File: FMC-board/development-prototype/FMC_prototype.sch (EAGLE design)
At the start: 68 parts, among them J1 DC_POWER_JACK-PJ-102AH, J2 DC_POWER_JACK-PJ-102AH

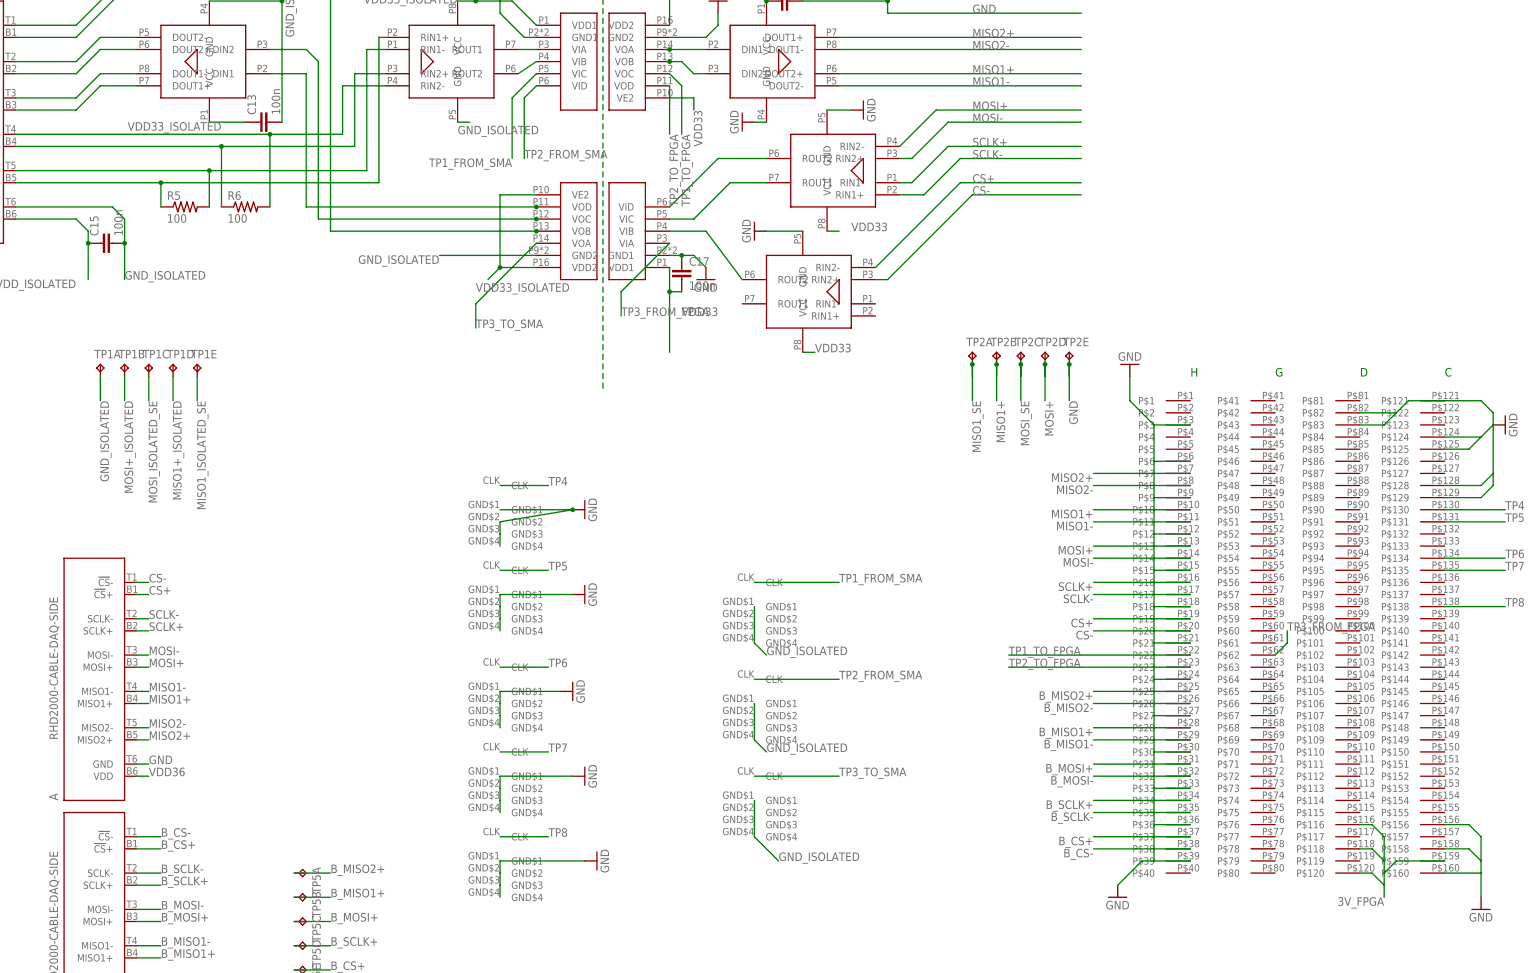
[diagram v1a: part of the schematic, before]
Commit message: clearing all but layer setup and silkscreen overlap warnings
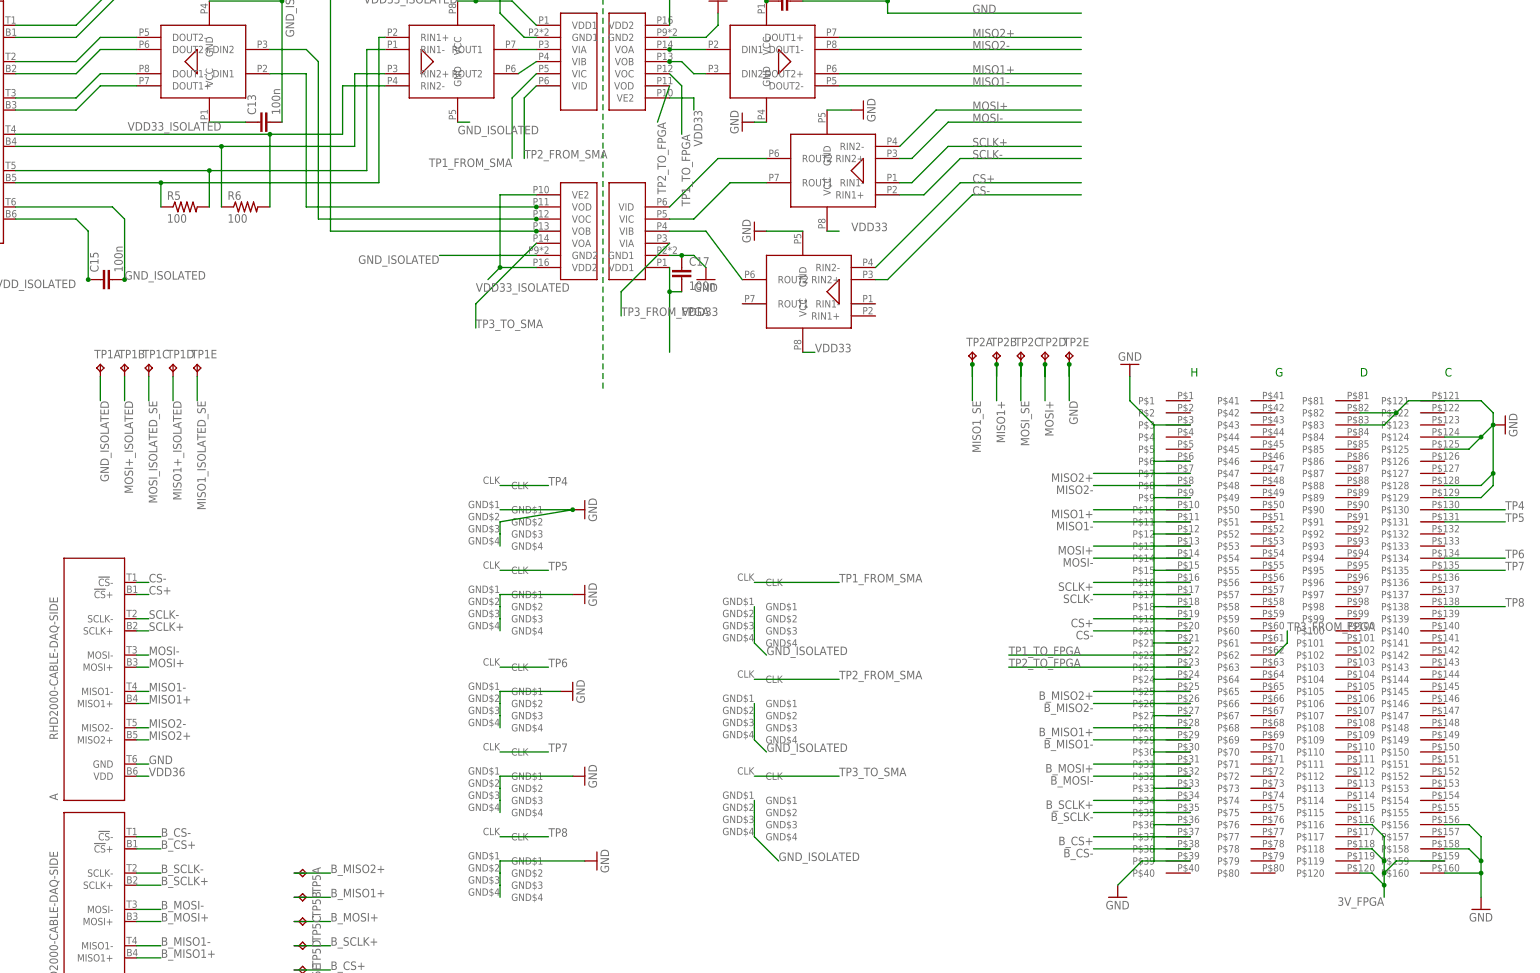
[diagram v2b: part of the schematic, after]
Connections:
- removed net GND4: C15.2
- net GND_ISOLATED: now also C15.2
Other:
- moved on the sheet: C15
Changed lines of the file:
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@@
 <instance part="C13" gate="C" x="91.44" y="203.2" rot="R90"/>
 <instance part="C14" gate="C" x="91.44" y="233.68" rot="R90"/>
-<instance part="C15" gate="C" x="58.42" y="177.8" rot="R90"/>
+<instance part="C15" gate="C" x="58.42" y="170.18" rot="R90"/>
 <instance part="C16" gate="C" x="137.16" y="233.68" rot="R180"/>
 <instance part="C17" gate="C" x="180.34" y="172.72"/>
@@
 <wire x1="63.5" y1="182.88" x2="60.96" y2="185.42" width="0.1524" layer="91"/>
 <label x="63.5" y="170.18" size="1.778" layer="95"/>
-<wire x1="63.5" y1="182.88" x2="63.5" y2="170.18" width="0.1524" layer="91"/>
+<wire x1="63.5" y1="182.88" x2="63.5" y2="172.72" width="0.1524" layer="91"/>
 <pinref part="A_ISOLATED" gate="A" pin="GND"/>
 <wire x1="60.96" y1="185.42" x2="40.64" y2="185.42" width="0.1524" layer="91"/>
+<pinref part="C15" gate="C" pin="2"/>
+<junction x="63.5" y="170.18"/>
+<wire x1="63.5" y1="172.72" x2="63.5" y2="170.18" width="0.1524" layer="91"/>
 </segment>
 <segment>
@@
 <net name="VDD_ISOLATED" class="0">
 <segment>
-<wire x1="55.88" y1="180.34" x2="55.88" y2="177.8" width="0.1524" layer="91"/>
-<wire x1="55.88" y1="177.8" x2="55.88" y2="170.18" width="0.1524" layer="91"/>
+<wire x1="55.88" y1="180.34" x2="55.88" y2="170.18" width="0.1524" layer="91"/>
 <wire x1="55.88" y1="180.34" x2="53.34" y2="182.88" width="0.1524" layer="91"/>
 <label x="53.34" y="170.18" size="1.778" layer="95" rot="R180"/>
 <pinref part="C15" gate="C" pin="1"/>
-<junction x="55.88" y="177.8"/>
+<junction x="55.88" y="170.18"/>
 <pinref part="A_ISOLATED" gate="A" pin="VDD"/>
 <wire x1="53.34" y1="182.88" x2="40.64" y2="182.88" width="0.1524" layer="91"/>
@@
 <wire x1="347.98" y1="45.72" x2="347.98" y2="40.64" width="0.1524" layer="91"/>
 <pinref part="GND15" gate="1" pin="GND"/>
+<junction x="347.98" y="48.26"/>
+<junction x="347.98" y="45.72"/>
 </segment>
 <segment>
@@
 <wire x1="322.58" y1="139.7" x2="327.66" y2="139.7" width="0.1524" layer="91"/>
 <wire x1="327.66" y1="139.7" x2="330.2" y2="142.24" width="0.1524" layer="91"/>
+<junction x="347.98" y="137.16"/>
+<junction x="350.52" y="129.54"/>
+<junction x="350.52" y="139.7"/>
+<junction x="330.2" y="142.24"/>
 </segment>
 <segment>
@@
 </segment>
 </net>
-<net name="GND4" class="0">
-<segment>
-<pinref part="C15" gate="C" pin="2"/>
-<junction x="63.5" y="177.8"/>
-</segment>
-</net>
 <net name="CS+_ISOLATED" class="0">
 <segment>
@@
 <wire x1="327.66" y1="43.18" x2="327.66" y2="40.64" width="0.1524" layer="91"/>
 <label x="327.66" y="40.64" size="1.778" layer="95" rot="R180"/>
+<junction x="327.66" y="48.26"/>
+<junction x="327.66" y="45.72"/>
+<junction x="327.66" y="43.18"/>
 </segment>
 <segment>
@@
 <segment>
 <pinref part="U$11" gate="G$1" pin="VOD"/>
-<wire x1="177.8" y1="210.82" x2="177.8" y2="200.66" width="0.1524" layer="91"/>
-<label x="177.8" y="200.66" size="1.778" layer="95" rot="R270"/>
-</segment>
-<segment>
+<wire x1="177.8" y1="210.82" x2="175.26" y2="203.2" width="0.1524" layer="91"/>
+<label x="175.26" y="203.2" size="1.778" layer="95" rot="R270"/>
+</segment>
+<segment>

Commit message: added optional DC DC converter
12V > 5V DC DC for powering headstage etc. can still be bypassed with jumper
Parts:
- added C1: 4.7uF, RHD2000_eval_board:C_0603
- added L1: 6.8uH, inductor-neosid:MS42
- added U$20: PDS1, open-ephys:PDS1
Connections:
- new net 12V_FPGA: C1.1, L1.1, U$4G$1.P$155, U$4G$1.P$157
- new net N$1: LINK-5V.3, U$20.+VO
- new net N$2: L1.2, U$20.VIN
- net GND: now also C1.2, U$20.GND
- net GND_ISOLATED: now also U$20.0V
- net VDD_IN: now also LINK-5V.1; no longer LINK-5V.2
- net VDD_ISOLATED: now also LINK-5V.2; no longer LINK-5V.1
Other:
- note added: "12V to 5V DC-Dc"
- note removed: "boost power supply input to +5.0V"
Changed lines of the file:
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@@
 <layers>
 <layer number="1" name="Top" color="4" fill="1" visible="no" active="no"/>
+<layer number="2" name="Route2" color="1" fill="3" visible="no" active="no"/>
+<layer number="3" name="Route3" color="4" fill="3" visible="no" active="no"/>
+<layer number="4" name="Route4" color="1" fill="4" visible="no" active="no"/>
+<layer number="5" name="Route5" color="4" fill="4" visible="no" active="no"/>
+<layer number="6" name="Route6" color="1" fill="8" visible="no" active="no"/>
+<layer number="7" name="Route7" color="4" fill="8" visible="no" active="no"/>
+<layer number="8" name="Route8" color="1" fill="2" visible="no" active="no"/>
+<layer number="9" name="Route9" color="4" fill="2" visible="no" active="no"/>
+<layer number="10" name="Route10" color="1" fill="7" visible="no" active="no"/>
+<layer number="11" name="Route11" color="4" fill="7" visible="no" active="no"/>
+<layer number="12" name="Route12" color="1" fill="5" visible="no" active="no"/>
+<layer number="13" name="Route13" color="4" fill="5" visible="no" active="no"/>
+<layer number="14" name="Route14" color="1" fill="6" visible="no" active="no"/>
+<layer number="15" name="Route15" color="4" fill="6" visible="no" active="no"/>
 <layer number="16" name="Bottom" color="1" fill="1" visible="no" active="no"/>
 <layer number="17" name="Pads" color="2" fill="1" visible="no" active="no"/>
@@
 <part name="U$18" library="SA_BB" deviceset="SMA_JACK_142-0701-201_DEV" device=""/>
 <part name="U$19" library="SA_BB" deviceset="SMA_JACK_142-0701-201_DEV" device=""/>
+<part name="L1" library="inductor-neosid" deviceset="MS42" device="" value="6.8uH"/>
+<part name="C1" library="RHD2000_eval_board" deviceset="C" device="_0603" value="4.7uF"/>
+<part name="U$20" library="open-ephys" deviceset="PDS1" device=""/>
 </parts>
 <sheets>
@@
 <text x="144.78" y="318.77" size="1.778" layer="91">headstage side</text>
 <text x="166.37" y="318.77" size="1.778" layer="91">aq. board side</text>
-<text x="254" y="279.4" size="2.54" layer="91" rot="R180">boost power supply input to +5.0V</text>
 <text x="35.56" y="337.82" size="2.54" layer="91">3.3V reg. for RHD side supply</text>
 <text x="193.04" y="269.24" size="2.54" layer="91">3.3V reg for aq board side supply</text>
@@
 <text x="304.8" y="149.86" size="1.778" layer="91">G</text>
 <text x="287.02" y="149.86" size="1.778" layer="91">H</text>
+<text x="226.06" y="312.42" size="1.778" layer="91">12V to 5V DC-Dc</text>
 </plain>
 <instances>
@@
 <instance part="U$18" gate="G$1" x="228.6" y="48.26"/>
 <instance part="U$19" gate="G$1" x="228.6" y="88.9"/>
+<instance part="L1" gate="G$1" x="213.36" y="307.34" rot="R90"/>
+<instance part="C1" gate="C" x="215.9" y="297.18" rot="R90"/>
+<instance part="U$20" gate="G$1" x="213.36" y="325.12" rot="R180"/>
 </instances>
 <busses>
@@
 <label x="198.12" y="91.44" size="1.778" layer="95"/>
 </segment>
+<segment>
+<wire x1="208.28" y1="325.12" x2="208.28" y2="337.82" width="0.1524" layer="91"/>
+<wire x1="208.28" y1="337.82" x2="203.2" y2="337.82" width="0.1524" layer="91"/>
+<label x="203.2" y="337.82" size="1.778" layer="95" rot="R90"/>
+<pinref part="U$20" gate="G$1" pin="0V"/>
+</segment>
 </net>
 <net name="VDD_ISOLATED" class="0">
@@
 <wire x1="121.92" y1="289.56" x2="121.92" y2="350.52" width="0.1524" layer="91"/>
 <pinref part="J2" gate="A" pin="PWR"/>
-<pinref part="LINK-5V" gate="1" pin="1"/>
-<wire x1="121.92" y1="350.52" x2="154.94" y2="350.52" width="0.1524" layer="91"/>
-<wire x1="154.94" y1="350.52" x2="162.56" y2="358.14" width="0.1524" layer="91"/>
+<wire x1="121.92" y1="350.52" x2="165.1" y2="350.52" width="0.1524" layer="91"/>
+<pinref part="LINK-5V" gate="1" pin="2"/>
+<wire x1="165.1" y1="350.52" x2="165.1" y2="358.14" width="0.1524" layer="91"/>
 </segment>
 <segment>
@@
 <wire x1="251.46" y1="289.56" x2="251.46" y2="287.02" width="0.1524" layer="91"/>
 <pinref part="J1" gate="A" pin="GND1"/>
-<wire x1="251.46" y1="287.02" x2="175.26" y2="287.02" width="0.1524" layer="91"/>
+<wire x1="251.46" y1="287.02" x2="220.98" y2="287.02" width="0.1524" layer="91"/>
 <pinref part="GND12" gate="1" pin="GND"/>
 <pinref part="LINK_GNDS" gate="1" pin="2"/>
+<wire x1="220.98" y1="287.02" x2="175.26" y2="287.02" width="0.1524" layer="91"/>
 <wire x1="175.26" y1="287.02" x2="175.26" y2="320.04" width="0.1524" layer="91"/>
 <wire x1="175.26" y1="320.04" x2="165.1" y2="330.2" width="0.1524" layer="91"/>
+<wire x1="218.44" y1="325.12" x2="220.98" y2="297.18" width="0.1524" layer="91"/>
+<pinref part="C1" gate="C" pin="2"/>
+<wire x1="220.98" y1="297.18" x2="220.98" y2="287.02" width="0.1524" layer="91"/>
+<junction x="220.98" y="297.18"/>
+<pinref part="U$20" gate="G$1" pin="GND"/>
 </segment>
 <segment>
@@
 <wire x1="185.42" y1="256.54" x2="187.96" y2="256.54" width="0.1524" layer="91"/>
 <pinref part="J1" gate="A" pin="PWR"/>
-<pinref part="LINK-5V" gate="1" pin="2"/>
 <wire x1="180.34" y1="284.48" x2="180.34" y2="342.9" width="0.1524" layer="91"/>
-<wire x1="180.34" y1="342.9" x2="165.1" y2="358.14" width="0.1524" layer="91"/>
 <junction x="180.34" y="284.48"/>
+<pinref part="LINK-5V" gate="1" pin="1"/>
+<wire x1="180.34" y1="342.9" x2="177.8" y2="342.9" width="0.1524" layer="91"/>
+<wire x1="177.8" y1="342.9" x2="162.56" y2="358.14" width="0.1524" layer="91"/>
 </segment>
 <segment>
@@
 </segment>
 </net>
+<net name="12V_FPGA" class="0">
+<segment>
+<pinref part="U$4" gate="G$1" pin="P$157"/>
+<wire x1="340.36" y1="53.34" x2="345.44" y2="58.42" width="0.1524" layer="91"/>
+<pinref part="U$4" gate="G$1" pin="P$155"/>
+<wire x1="340.36" y1="58.42" x2="345.44" y2="58.42" width="0.1524" layer="91"/>
+<wire x1="345.44" y1="58.42" x2="350.52" y2="58.42" width="0.1524" layer="91"/>
+<label x="350.52" y="58.42" size="1.778" layer="95"/>
+<label x="350.52" y="58.42" size="1.778" layer="95"/>
+</segment>
+<segment>
+<wire x1="213.36" y1="302.26" x2="213.36" y2="297.18" width="0.1524" layer="91"/>
+<label x="213.36" y="294.64" size="1.778" layer="95" rot="R180"/>
+<pinref part="L1" gate="G$1" pin="1"/>
+<pinref part="C1" gate="C" pin="1"/>
+<wire x1="213.36" y1="297.18" x2="213.36" y2="294.64" width="0.1524" layer="91"/>
+</segment>
+</net>
+<net name="N$2" class="0">
+<segment>
+<pinref part="L1" gate="G$1" pin="2"/>
+<wire x1="213.36" y1="312.42" x2="213.36" y2="325.12" width="0.1524" layer="91"/>
+<pinref part="U$20" gate="G$1" pin="VIN"/>
+</segment>
+</net>
+<net name="N$1" class="0">
+<segment>
+<pinref part="U$20" gate="G$1" pin="+VO"/>
+<wire x1="203.2" y1="325.12" x2="203.2" y2="330.2" width="0.1524" layer="91"/>
+<wire x1="203.2" y1="330.2" x2="190.5" y2="342.9" width="0.1524" layer="91"/>
+<pinref part="LINK-5V" gate="1" pin="3"/>
+<wire x1="190.5" y1="342.9" x2="182.88" y2="342.9" width="0.1524" layer="91"/>
+<wire x1="182.88" y1="342.9" x2="167.64" y2="358.14" width="0.1524" layer="91"/>
+</segment>
+</net>

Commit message: Cleaning up schematic as a means to understand and verify it.
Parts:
- removed 5VD: TPS79301, RHD2000_eval_board:TPS79301
- removed C53: 15p, RHD2000_eval_board:C_0603
- removed R72: 30.9k, RHD2000_eval_board:R_0603
- removed R73: 95.3k, RHD2000_eval_board:R_0603
- added U1: TPS79333, jonnew:TPS79333
- J2: value DC_POWER_JACK-PJ-102AH -> PJ-102AH
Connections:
- net VDD33 renamed +3V3
- net VDD36 renamed +3V6
- net VDD_ISOLATED renamed VDD_ISO
- removed net GND_ISOLATED: 5VD.GND, 5VD2.GND, A_ISOLATED.GND, C13.2, C14.2, C15.2, C16.2, C51.2, C52.2, C54.2, C6.2, C7.2, C9.2, J2.GND1, J2.GND2, LINK_GNDS.1, R3.2, R72.2, TP1A.TP, TP3A.TP, TP3E.TP, U$11.GND1, U$12.GND2, U$17.GND$1, U$17.GND$2, U$17.GND$3, U$17.GND$4, U$18.GND$1, U$18.GND$2, U$18.GND$3, U$18.GND$4, U$19.GND$1, U$19.GND$2, U$19.GND$3, U$19.GND$4, U$20.0V, U$6.GND, U$7.GND, U$9.GND
- removed net N$108: 5VD.FB, C53.2, R72.1, R73.1
- removed net N$3: LINK_FPGA_3V.3
- removed net VDD33_ISOLATED: 5VD.OUT, C13.1, C14.1, C16.1, C53.1, C54.1, R73.2, TP3C.TP, U$11.VDD1, U$12.VDD2, U$12.VE2, U$6.VCC, U$7.VCC, U$9.VCC
- new net 5V_ISO: TP3D.TP
- new net GND_ISO: 5VD2.GND, A_ISOLATED.GND, C13.2, C14.2, C15.2, C16.2, C51.2, C52.2, C54.2, C6.2, C7.2, C9.2, J2.GND1, J2.GND2, LINK_GNDS.1, R3.2, TP1A.TP, TP3A.TP, TP3E.TP, U$11.GND1, U$12.GND2, U$17.GND$1, U$17.GND$2, U$17.GND$3, U$17.GND$4, U$18.GND$1, U$18.GND$2, U$18.GND$3, U$18.GND$4, U$19.GND$1, U$19.GND$2, U$19.GND$3, U$19.GND$4, U$20.0V, U$6.GND, U$7.GND, U$9.GND, U1.GND
- new net VDD33_ISO: C13.1, C14.1, C16.1, C54.1, TP3C.TP, U$11.VDD1, U$12.VDD2, U$12.VE2, U$6.VCC, U$7.VCC, U$9.VCC, U1.OUT
- net 5V_ISOLATED: now also U1.EN, U1.IN; no longer 5VD.EN, 5VD.IN, TP3D.TP
- net GND: now also U$4G$1.P$6
- net N$97: now also U1.NR; no longer 5VD.NR
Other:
- note added: "AQ. BOARD SIDE"
- note added: "HEADSTAGE SIDE"
- note added: "ISOLATED PWR TEST POINTS"
- note added: "NOMINAL PWR TEST POINTS"
- note removed: "aq. board side"
- note removed: "headstage side"
- moved on the sheet: 5VD1, 5VD2, 5VD4, A, A_ISOLATED, B, C1, C12, C13, C14, C15, C16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
